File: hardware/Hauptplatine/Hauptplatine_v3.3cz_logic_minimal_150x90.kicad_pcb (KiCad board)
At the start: 2 copper layers, 150 x 90 mm, 29 parts, among them J1 230V IN L/N/PE, J2 REED OFFEN, J3 REED GEKIPPT, J4 RS485 5V/GND/A/B, J5 MOTOR N/PE/AUF/AB, J6 28BYJ-48 OBEN, J7 28BYJ-48 UNTEN, K1 Finder 40.52.9.005.0000 AUF, K2 Finder 40.52.9.005.0000 AB, Q1 BC337 AUF, Q2 BC337 AB, U1 ESP32-S3 DevKitC-1 headers, U2 AMS1117-3.3, U3 MAX3485, U4 ULN2003A OBEN, U5 ULN2003A UNTEN

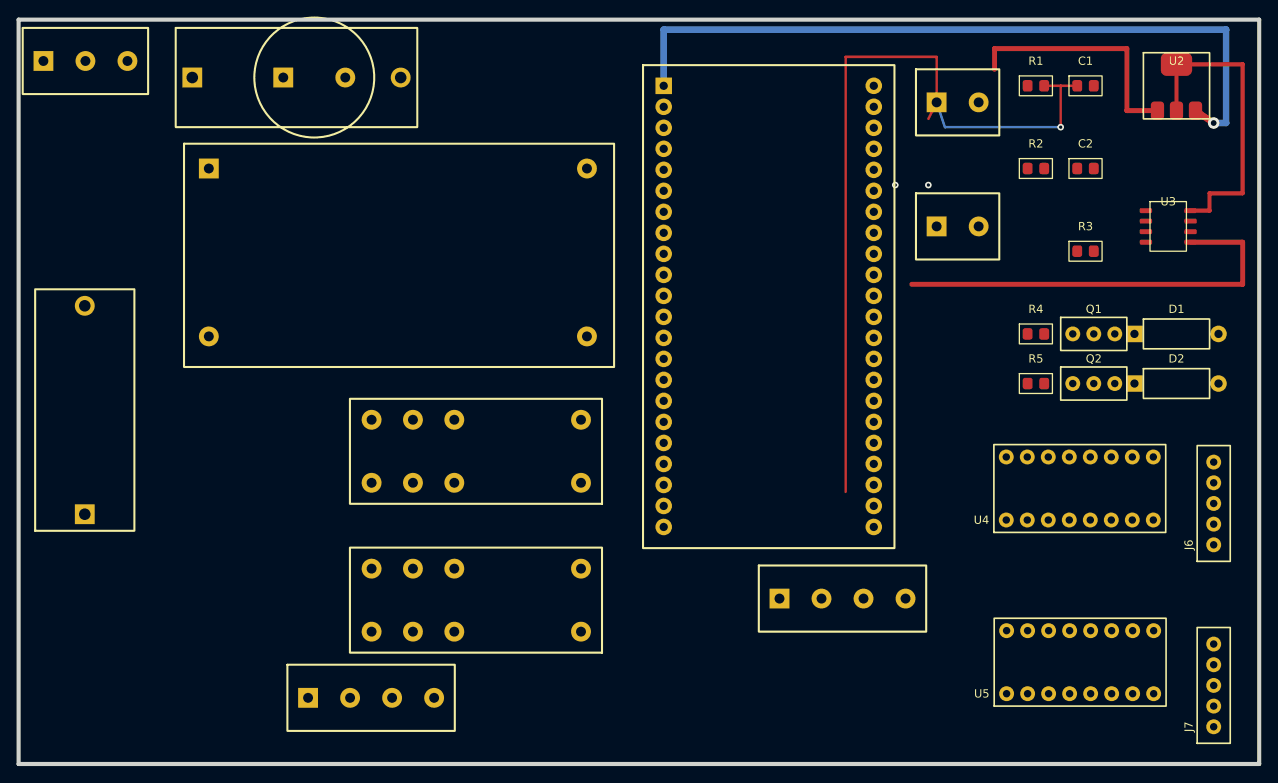
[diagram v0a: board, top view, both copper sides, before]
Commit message: Fix v3.3cz rebuild from cy: safe REED route and compact mains layout
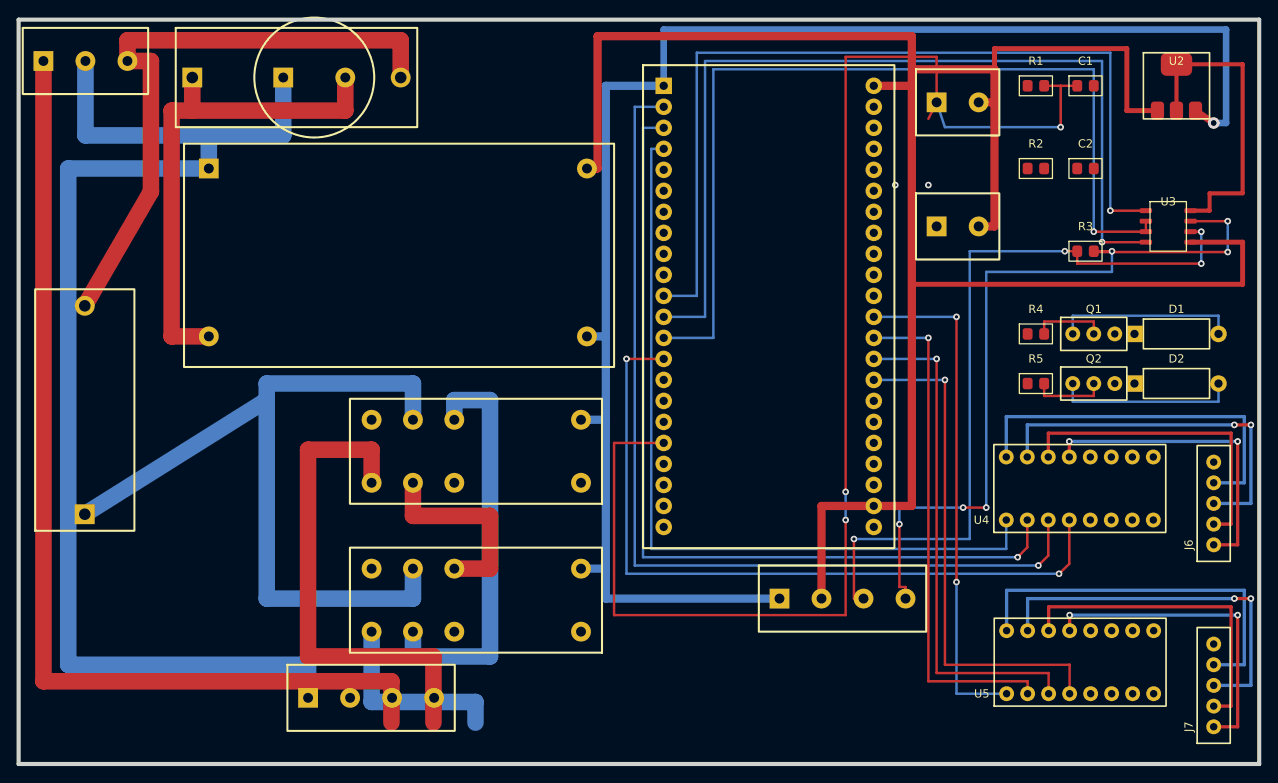
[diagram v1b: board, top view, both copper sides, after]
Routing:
- net /GND: track 81.1 -> 252.7 mm
- net /AC_N: track 0.00 -> 153.9 mm
- net /PE: track 0.00 -> 122.1 mm
- net /STEP_TOP_3: track 0.00 -> 113.8 mm, vias 0 -> 1
- net /RS485_DE: track 0.00 -> 111.7 mm, vias 0 -> 1
- net /RS485_TX: track 0.00 -> 111.2 mm, vias 0 -> 1
- net /RS485_RX: track 0.00 -> 106.8 mm, vias 0 -> 1
- net /STEP_TOP_2: track 0.00 -> 104.7 mm, vias 0 -> 1
- net /+5V: track 90.3 -> 188.5 mm
- net /STEP_TOP_1: track 0.00 -> 96.3 mm
- net /L_MOTOR: track 0.00 -> 95.3 mm
- net /RS485_B: track 0.00 -> 95.2 mm, vias 0 -> 6
- net /RS485_A: track 0.00 -> 91.8 mm, vias 0 -> 4
- net /STEP_TOP_4: track 0.00 -> 89.8 mm, vias 0 -> 2
- net /AC_L: track 0.00 -> 74.6 mm
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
